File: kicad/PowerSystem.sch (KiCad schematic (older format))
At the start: 0 parts

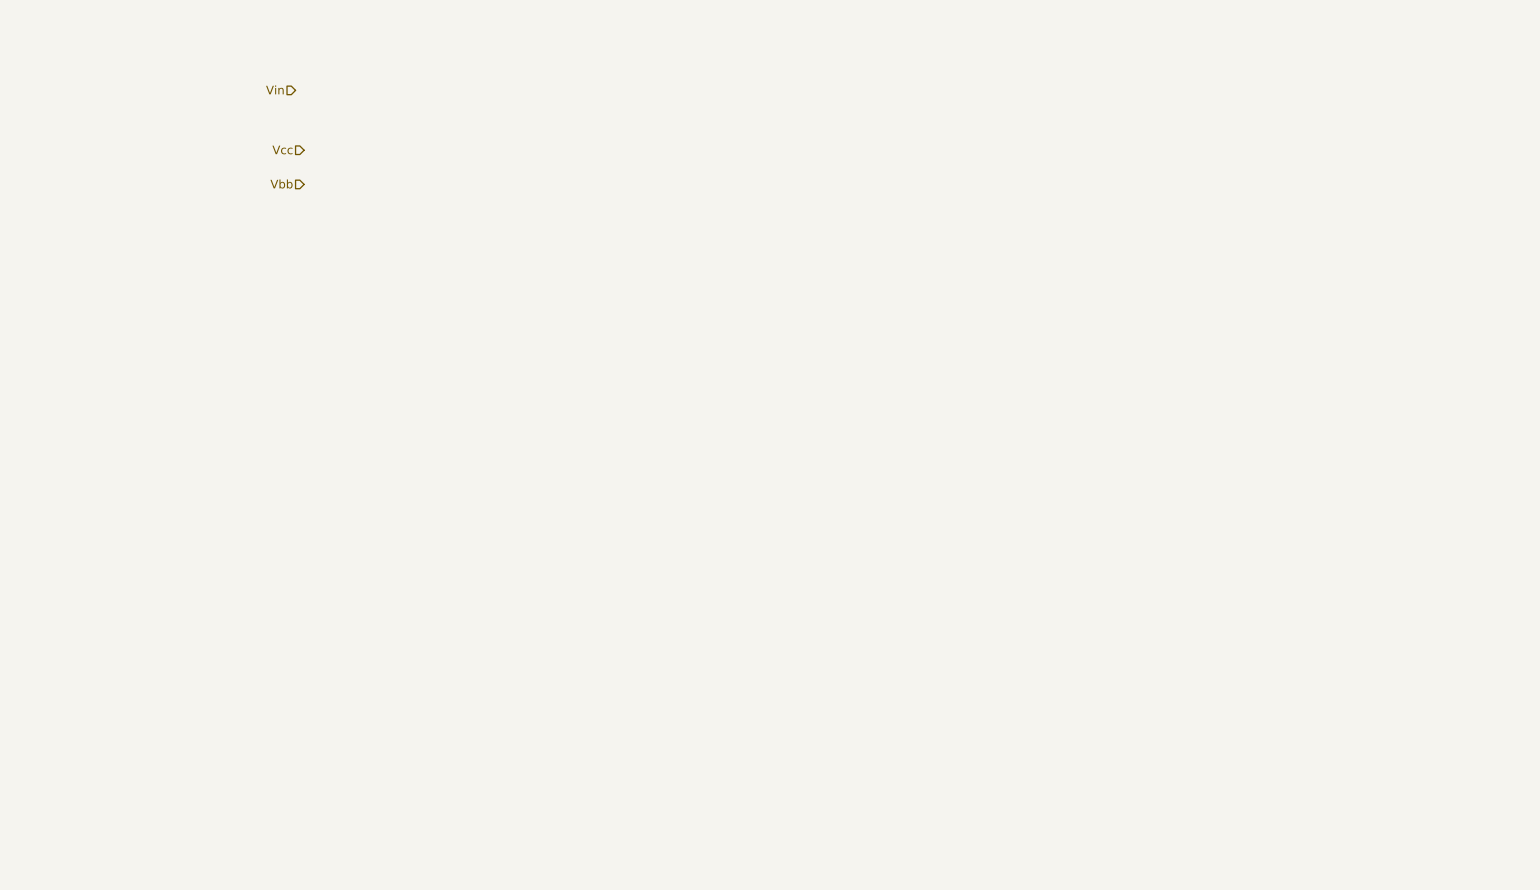
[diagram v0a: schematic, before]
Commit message: First draft of some of the sub-sheets
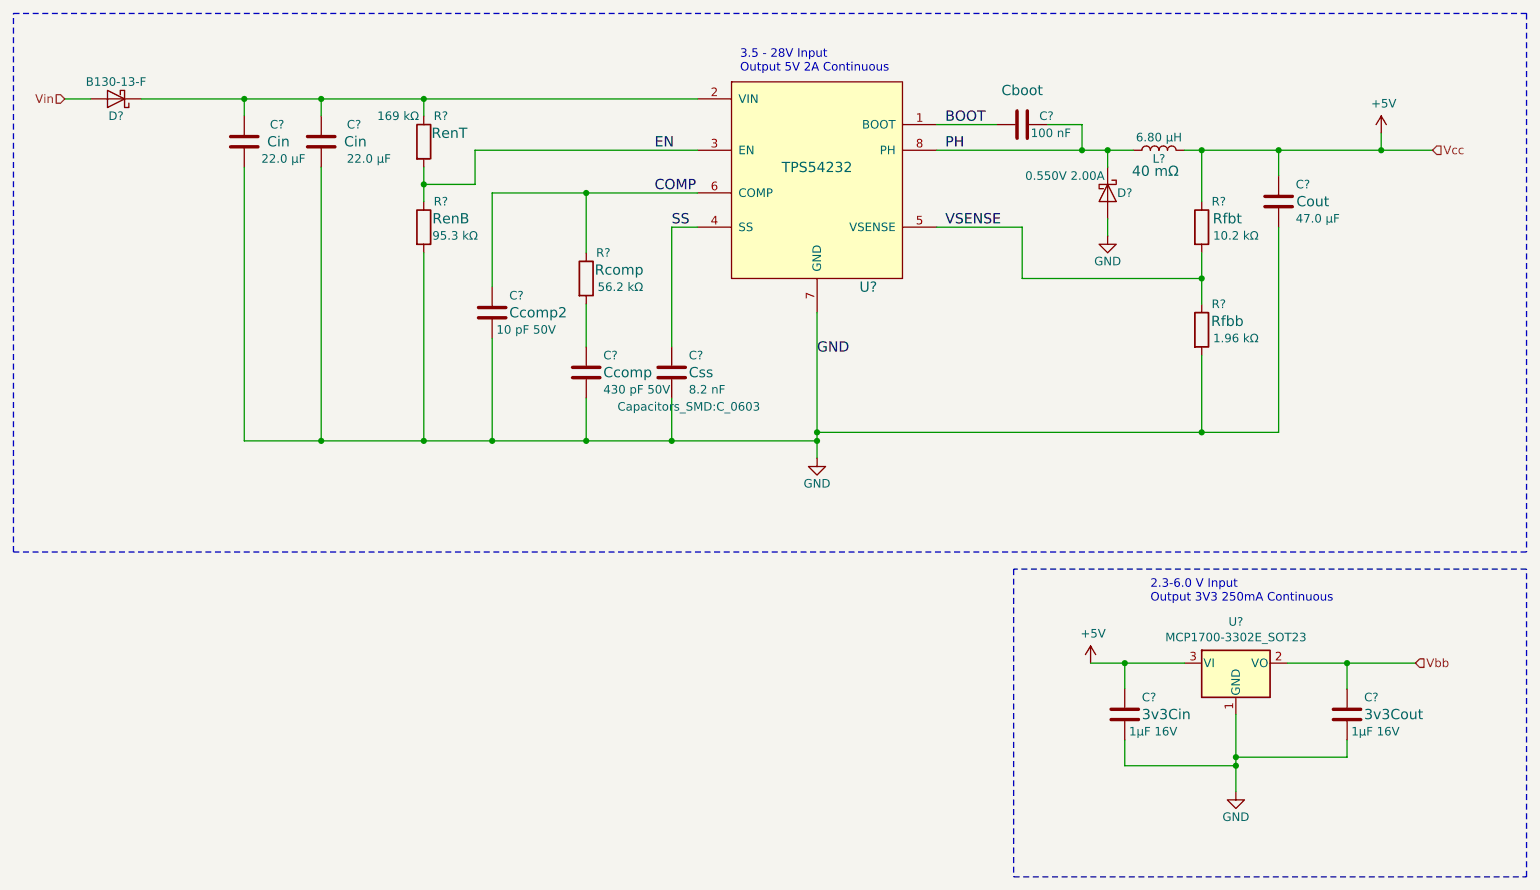
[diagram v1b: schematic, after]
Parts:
- added C? (x2): 22.0 μF, Capacitors_SMD:C_1210, symbol FieldDevice_Power_5V-rescue:C
- added C?: 10 pF 50V, Capacitors_SMD:C_0805, symbol FieldDevice_Power_5V-rescue:C
- added C?: 430 pF 50V, Capacitors_SMD:C_0805, symbol FieldDevice_Power_5V-rescue:C
- added C?: 8.2 nF, Capacitors_SMD:C_0603, symbol FieldDevice_Power_5V-rescue:C
- added C?: 100 nF, Capacitors_SMD:C_0805, symbol FieldDevice_Power_5V-rescue:C
- added C?: 47.0 μF, Capacitors_SMD:C_1206, symbol FieldDevice_Power_5V-rescue:C
- added C? (x2): 1μF 16V, Capacitors_SMD:C_0805, symbol FieldDevice_Power_5V-rescue:C
- added D?: 0.550V 2.00A, FieldDevice_Power_5V:D_SOD-123F, symbol FieldDevice_Power_5V-rescue:D_Schottky
- added D?: B130-13-F, FieldDevice_Power_5V:B130-13-F, symbol FieldDevice_Power_5V-rescue:D_Schottky
- added L?: 6.80 μΗ, FieldDevice_Power_5V:SDR0805-6R8ML, symbol FieldDevice_Power_5V-rescue:L
- added R?: 169 kΩ, Resistors_SMD:R_0805, symbol FieldDevice_Power_5V-rescue:R
- added R?: 95.3 kΩ, Resistors_SMD:R_0805, symbol FieldDevice_Power_5V-rescue:R
- added R?: 56.2 kΩ, Resistors_SMD:R_0805, symbol FieldDevice_Power_5V-rescue:R
- added R?: 10.2 kΩ, Resistors_SMD:R_0805, symbol FieldDevice_Power_5V-rescue:R
- added R?: 1.96 kΩ, Resistors_SMD:R_0805, symbol FieldDevice_Power_5V-rescue:R
- added U?: TPS54232, FieldDevice_Power_5V:TPS54232DR, symbol FieldDevice_Power_5V-rescue:TPS54232
- added U?: MCP1700-3302E_SOT23, Package_TO_SOT_SMD:SOT-23, symbol Regulator_Linear:MCP1700-3302E_SOT23
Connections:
- net Vbb: now also C?.1, U?.2 (VO)
- net Vin: now also D?.2 (A)
- new net: C?.1, C?.1, D?.1 (K), R?.1, U?.2 (VIN)
- new net: C?.1, R?.2
- new net +5V: C?.1, C?.1, L?.2, R?.1, U?.3 (VI)
- new net BOOT: C?.2, U?.1 (BOOT)
- new net COMP: C?.1, R?.1, U?.6 (COMP)
- new net EN: R?.1, R?.2, U?.3 (EN)
- new net GND: C?.2, C?.2, C?.2, C?.2, C?.2, C?.2, C?.2, C?.2, D?.2 (A), R?.2, R?.2, U?.1 (GND), U?.7 (GND)
- new net PH: C?.1, D?.1 (K), L?.1, U?.8 (PH)
- new net SS: C?.1, U?.4 (SS)
- new net VSENSE: R?.1, R?.2, U?.5 (VSENSE)
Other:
- note added: "2.3-6.0 V Input\nOutput 3V3 250mA Continuous"
- note added: "3.5 - 28V Input\nOutput 5V 2A Continuous"
